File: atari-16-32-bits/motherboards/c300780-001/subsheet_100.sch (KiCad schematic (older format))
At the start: 16 parts

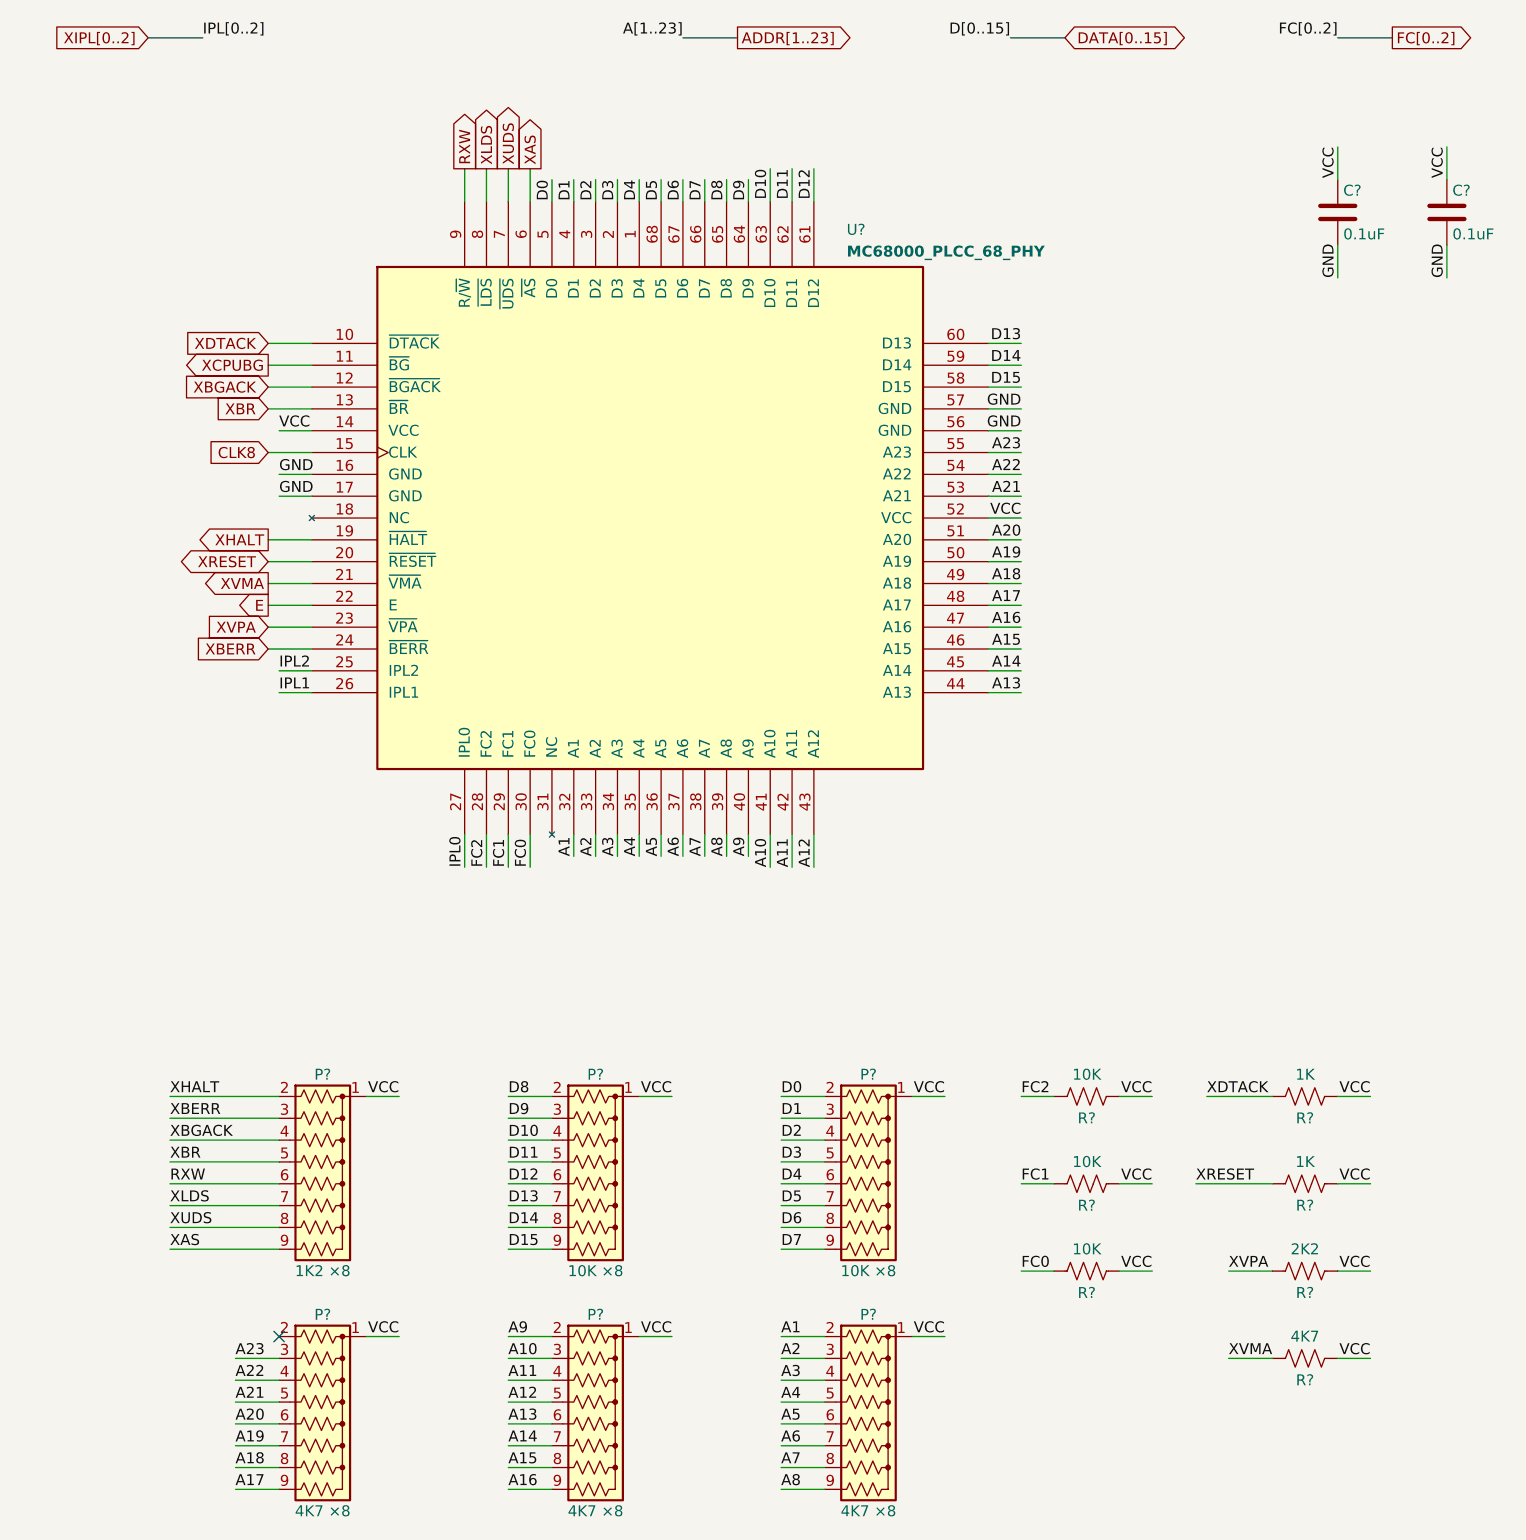
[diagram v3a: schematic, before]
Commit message: re-annotate component following move of subsheets in schematics
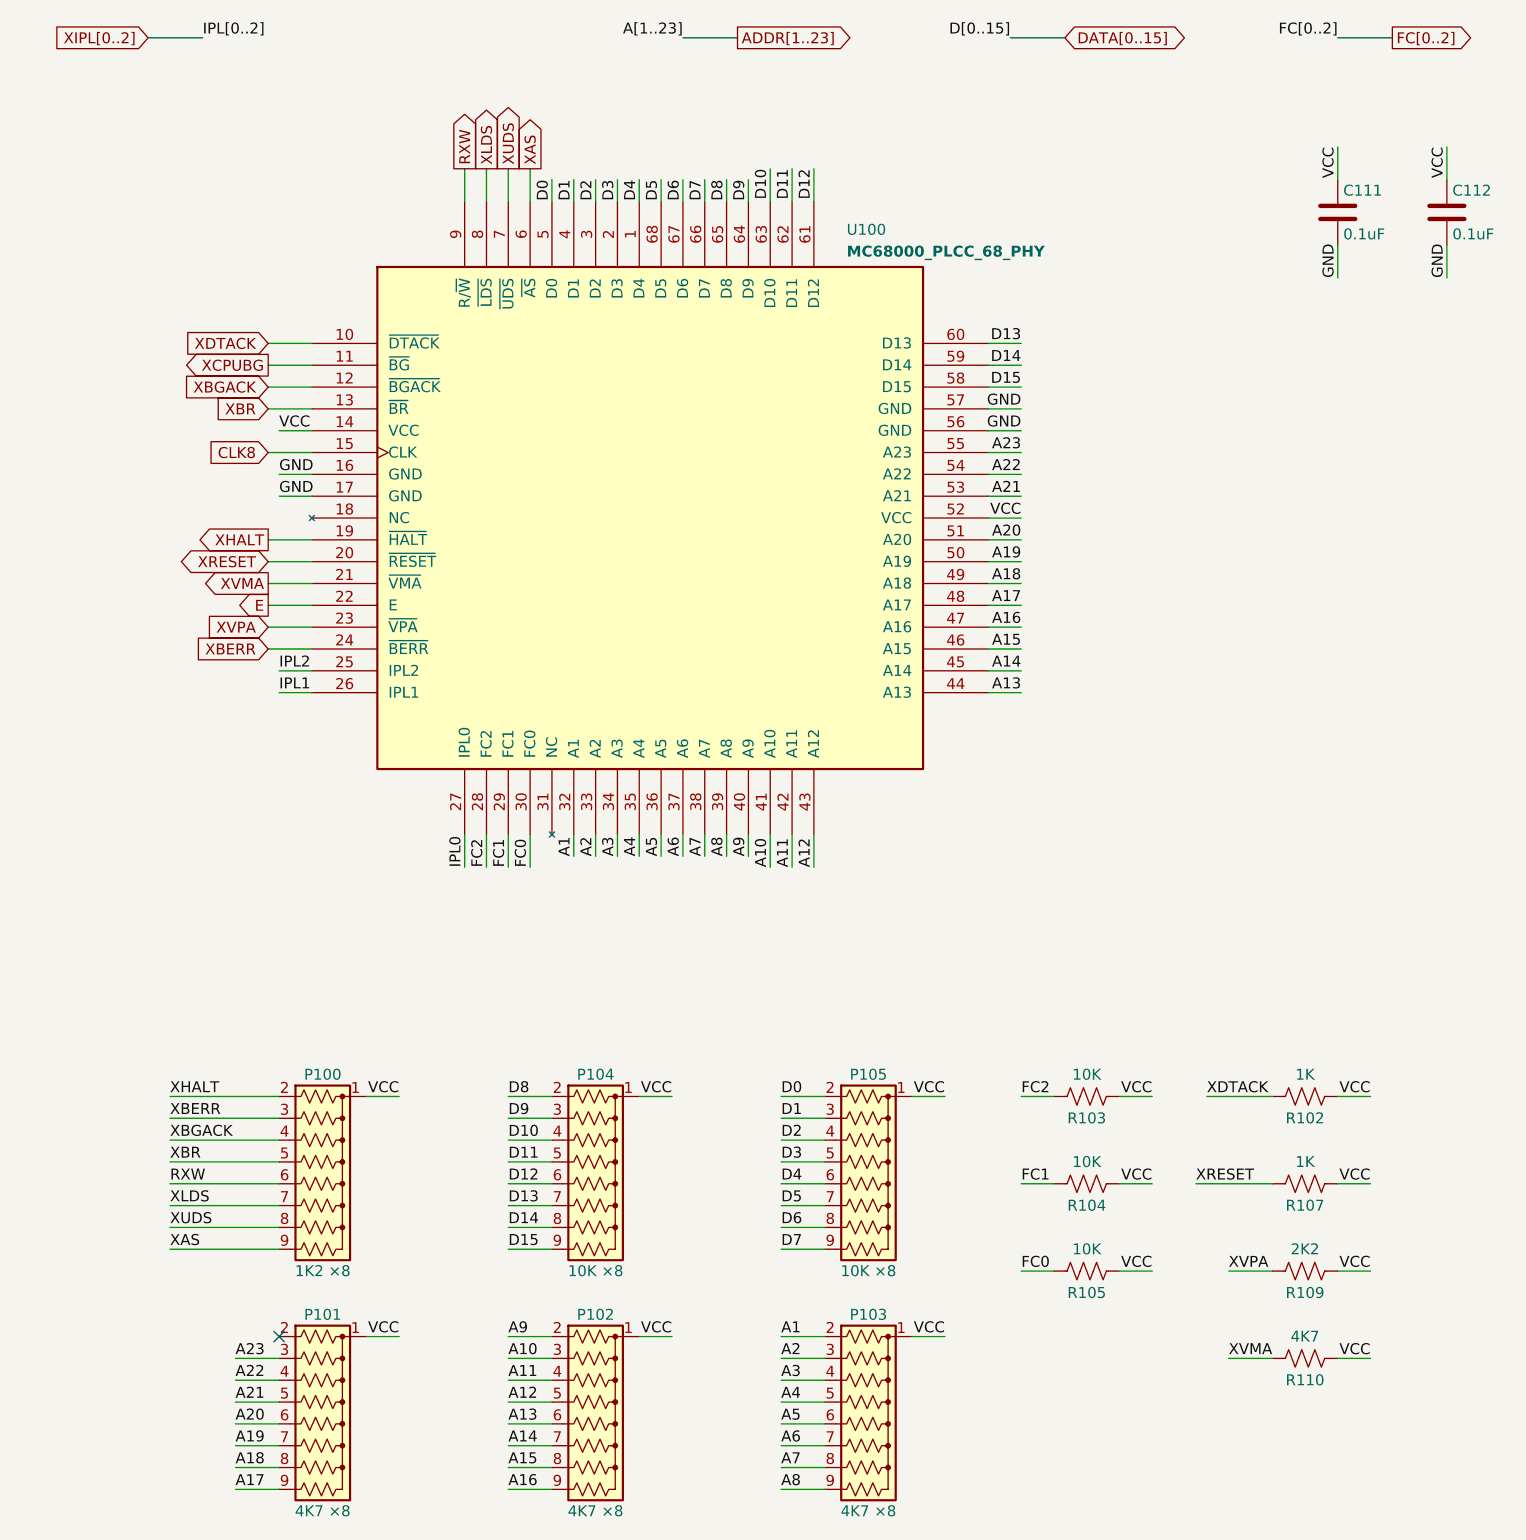
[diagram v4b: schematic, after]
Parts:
- gave numbers to parts that had none: 14
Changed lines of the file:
@@
 $Descr A4 8268 11693 portrait
 encoding utf-8
-Sheet 14 8
+Sheet 8 9
 Title ""
 Date ""
@@
 GND
 $Comp
-L mc_68000_plcc68:MC68000_PLCC_68_PHY U?
+L mc_68000_plcc68:MC68000_PLCC_68_PHY U100
 U 1 1 607B5358
 P 3600 3200
-F 0 "U?" H 4500 4550 50  0000 L TNN
+F 0 "U100" H 4500 4550 50  0000 L TNN
 F 1 "MC68000_PLCC_68_PHY" H 4500 4450 50  0000 L TNB
 F 2 "Package_LCC:PLCC-68_THT-Socket" H 4500 4650 50  0001 L TNN
@@
 AR Path="/60786F27/6078774E/607ECFCE" Ref="C?"  Part="1"
 AR Path="/60786F27/607874AD/607ECFCE" Ref="C111"  Part="1"
-AR Path="/6089D0C6/607ECFCE" Ref="C?"  Part="1"
-F 0 "C?" H 6775 1900 50  0000 L CNN
+AR Path="/6089D0C6/607ECFCE" Ref="C111"  Part="1"
+F 0 "C111" H 6775 1900 50  0000 L CNN
 F 1 "0.1uF" H 6775 1700 50  0000 L CNN
 F 2 "" H 6788 1650 50  0001 C CNN
@@
 AR Path="/60786F27/6078774E/607ECFD4" Ref="C?"  Part="1"
 AR Path="/60786F27/607874AD/607ECFD4" Ref="C112"  Part="1"
-AR Path="/6089D0C6/607ECFD4" Ref="C?"  Part="1"
-F 0 "C?" H 7275 1900 50  0000 L CNN
+AR Path="/6089D0C6/607ECFD4" Ref="C112"  Part="1"
+F 0 "C112" H 7275 1900 50  0000 L CNN
 F 1 "0.1uF" H 7275 1700 50  0000 L CNN
 F 2 "" H 7288 1650 50  0001 C CNN
@@
 	7250 1500 7250 1650
 $Comp
-L Device:R_Network08_US P?
+L Device:R_Network08_US P100
 U 1 1 607F5888
 P 2100 6250
-F 0 "P?" V 1600 6250 50  0000 C CNN
+F 0 "P100" V 1600 6250 50  0000 C CNN
 F 1 "1K2 ×8" V 2500 6250 50  0000 C CNN
 F 2 "Resistor_THT:R_Array_SIP9" V 2575 6250 50  0001 C CNN
@@
 $EndComp
 $Comp
-L Device:R_Network08_US P?
+L Device:R_Network08_US P101
 U 1 1 607F7061
 P 2100 7350
-F 0 "P?" V 1600 7350 50  0000 C CNN
+F 0 "P101" V 1600 7350 50  0000 C CNN
 F 1 "4K7 ×8" V 2500 7350 50  0000 C CNN
 F 2 "Resistor_THT:R_Array_SIP9" V 2575 7350 50  0001 C CNN
@@
 $EndComp
 $Comp
-L Device:R_Network08_US P?
+L Device:R_Network08_US P102
 U 1 1 607F8D98
 P 3350 7350
-F 0 "P?" V 2850 7350 50  0000 C CNN
+F 0 "P102" V 2850 7350 50  0000 C CNN
 F 1 "4K7 ×8" V 3750 7350 50  0000 C CNN
 F 2 "Resistor_THT:R_Array_SIP9" V 3825 7350 50  0001 C CNN
@@
 $EndComp
 $Comp
-L Device:R_Network08_US P?
+L Device:R_Network08_US P103
 U 1 1 607F991C
 P 4600 7350
-F 0 "P?" V 4100 7350 50  0000 C CNN
+F 0 "P103" V 4100 7350 50  0000 C CNN
 F 1 "4K7 ×8" V 5000 7350 50  0000 C CNN
 F 2 "Resistor_THT:R_Array_SIP9" V 5075 7350 50  0001 C CNN
@@
 $EndComp
 $Comp
-L Device:R_Network08_US P?
+L Device:R_Network08_US P104
 U 1 1 607FB176
 P 3350 6250
-F 0 "P?" V 2850 6250 50  0000 C CNN
+F 0 "P104" V 2850 6250 50  0000 C CNN
 F 1 "10K ×8" V 3750 6250 50  0000 C CNN
 F 2 "Resistor_THT:R_Array_SIP9" V 3825 6250 50  0001 C CNN
@@
 $EndComp
 $Comp
-L Device:R_Network08_US P?
+L Device:R_Network08_US P105
 U 1 1 60815C70
 P 4600 6250
-F 0 "P?" V 4100 6250 50  0000 C CNN
+F 0 "P105" V 4100 6250 50  0000 C CNN
 F 1 "10K ×8" V 5000 6250 50  0000 C CNN
 F 2 "Resistor_THT:R_Array_SIP9" V 5075 6250 50  0001 C CNN
@@
 NoConn ~ 1900 6950
 $Comp
-L Device:R_US R?
+L Device:R_US R102
 U 1 1 60907E08
 P 6600 5850
-F 0 "R?" V 6700 5850 50  0000 C CNN
+F 0 "R102" V 6700 5850 50  0000 C CNN
 F 1 "1K" V 6500 5850 50  0000 C CNN
 F 2 "" V 6640 5840 50  0001 C CNN
@@
 $EndComp
 $Comp
-L Device:R_US R?
+L Device:R_US R103
 U 1 1 6090DB64
 P 5600 5850
-F 0 "R?" V 5700 5850 50  0000 C CNN
+F 0 "R103" V 5700 5850 50  0000 C CNN
 F 1 "10K" V 5500 5850 50  0000 C CNN
 F 2 "" V 5640 5840 50  0001 C CNN
@@
 $EndComp
 $Comp
-L Device:R_US R?
+L Device:R_US R104
 U 1 1 6090DFB5
 P 5600 6250
-F 0 "R?" V 5700 6250 50  0000 C CNN
+F 0 "R104" V 5700 6250 50  0000 C CNN
 F 1 "10K" V 5500 6250 50  0000 C CNN
 F 2 "" V 5640 6240 50  0001 C CNN
@@
 $EndComp
 $Comp
-L Device:R_US R?
+L Device:R_US R105
 U 1 1 6090EA19
 P 5600 6650
-F 0 "R?" V 5700 6650 50  0000 C CNN
+F 0 "R105" V 5700 6650 50  0000 C CNN
 F 1 "10K" V 5500 6650 50  0000 C CNN
 F 2 "" V 5640 6640 50  0001 C CNN
@@
 	5750 6650 5900 6650
 $Comp
-L Device:R_US R?
+L Device:R_US R107
 U 1 1 6093D9ED
 P 6600 6250
-F 0 "R?" V 6700 6250 50  0000 C CNN
+F 0 "R107" V 6700 6250 50  0000 C CNN
 F 1 "1K" V 6500 6250 50  0000 C CNN
 F 2 "" V 6640 6240 50  0001 C CNN
@@
 $EndComp
 $Comp
-L Device:R_US R?
+L Device:R_US R109
 U 1 1 6093E40C
 P 6600 6650
-F 0 "R?" V 6700 6650 50  0000 C CNN
+F 0 "R109" V 6700 6650 50  0000 C CNN
 F 1 "2K2" V 6500 6650 50  0000 C CNN
 F 2 "" V 6640 6640 50  0001 C CNN
@@
 $EndComp
 $Comp
-L Device:R_US R?
+L Device:R_US R110
 U 1 1 6093E522
 P 6600 7050
-F 0 "R?" V 6700 7050 50  0000 C CNN
+F 0 "R110" V 6700 7050 50  0000 C CNN
 F 1 "4K7" V 6500 7050 50  0000 C CNN
 F 2 "" V 6640 7040 50  0001 C CNN
